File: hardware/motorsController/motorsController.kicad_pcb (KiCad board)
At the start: 2 copper layers, 181 x 55.5 mm, 80 parts, among them J1 batery_connector, J10 batery_connector, J11 Conn_01x04, J2 Screw_Terminal_01x01, J3 Screw_Terminal_01x01, J4 Screw_Terminal_01x01, J5 Screw_Terminal_01x01, J6 Screw_Terminal_01x01, J7 Screw_Terminal_01x01, J8 Screw_Terminal_01x01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

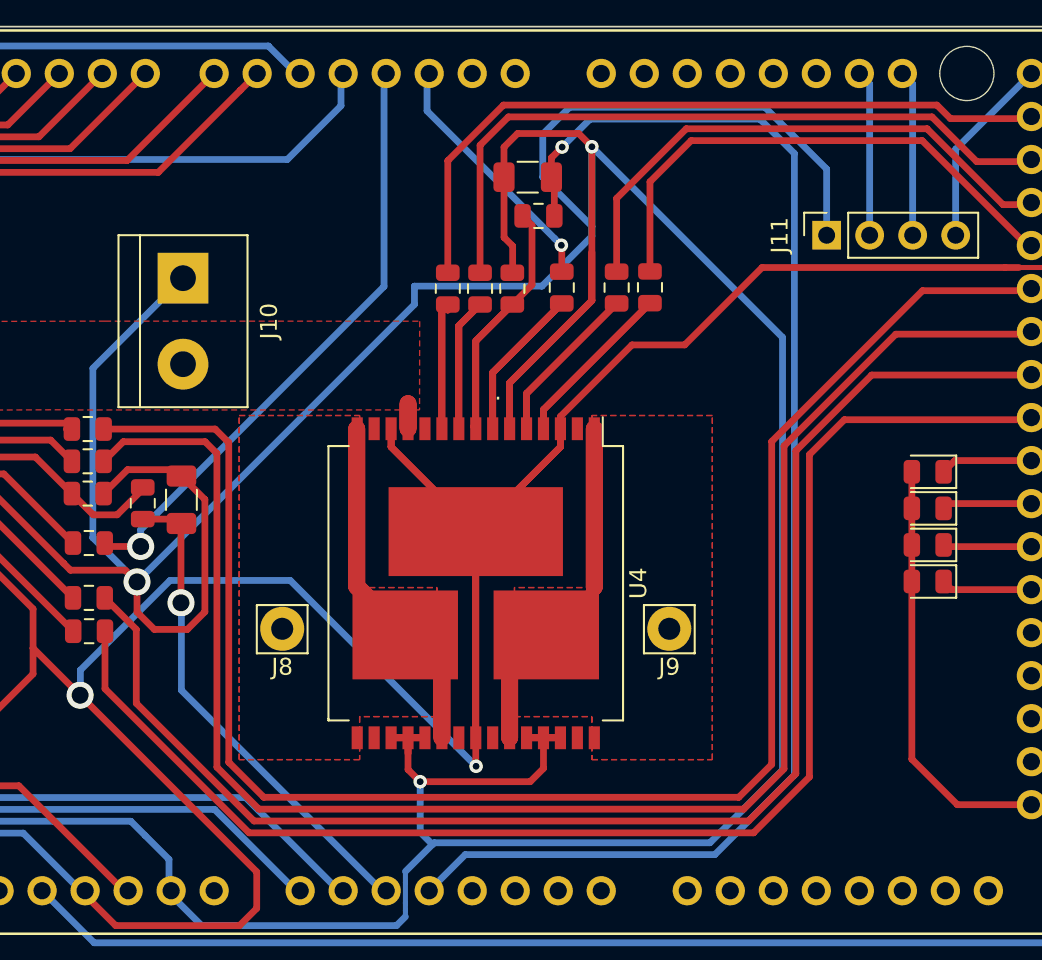
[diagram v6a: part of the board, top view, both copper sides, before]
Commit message: increase vias' dieamter for rear-left driver
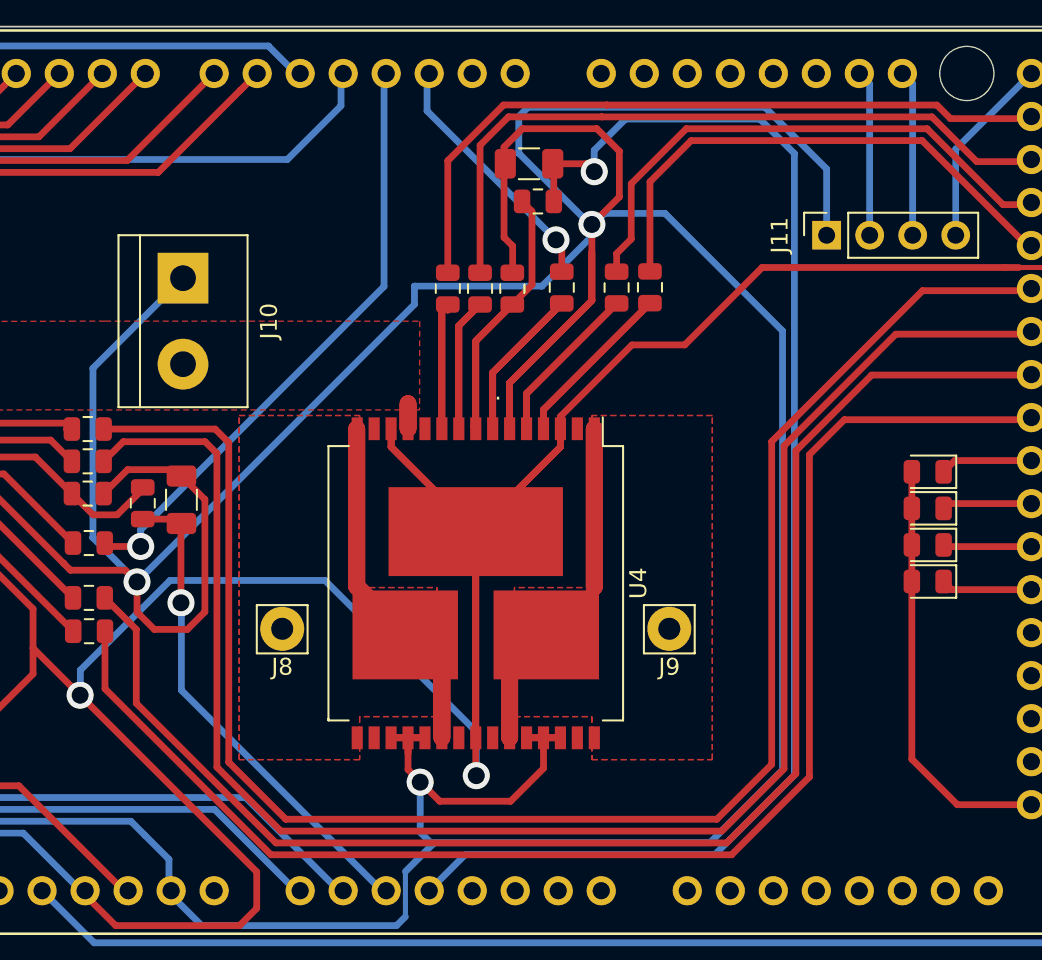
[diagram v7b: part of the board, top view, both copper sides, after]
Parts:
- moved R22 0.86 mm to (162.1, 34.5)
- moved C4 0.80 mm to (161.6, 32.2)
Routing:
- net +5V: track 422.7 -> 425.0 mm
- net /motor_right_rear_diag_b: track 97.8 -> 98.8 mm
- net /motor_right_rear_fwd: track 82.8 -> 83.8 mm
- net /motor_right_rear_diag_a: track 84.7 -> 85.8 mm
- net /motor_right_rear_back: track 98.3 -> 99.4 mm
- net Net-(R22-Pad1): track 22.8 -> 23.6 mm
- net /motor_left_rear_pwm: track 14.9 -> 15.5 mm

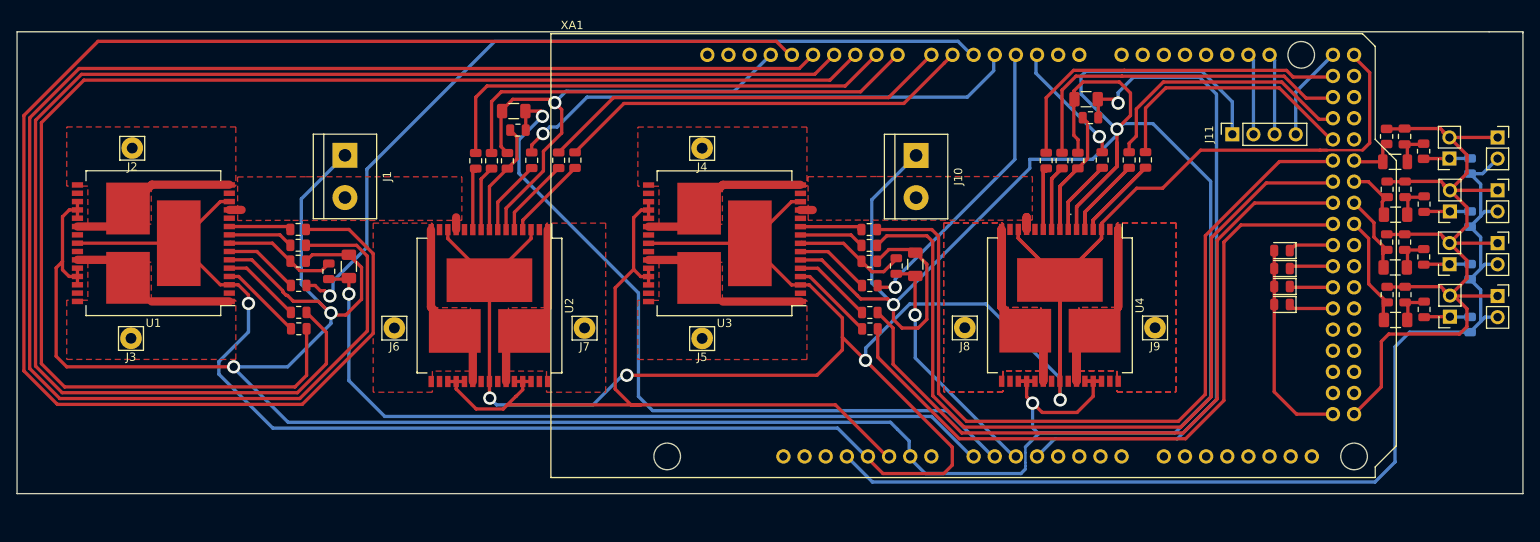
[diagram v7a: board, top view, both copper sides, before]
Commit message: layout a pcb for testing a motor driver
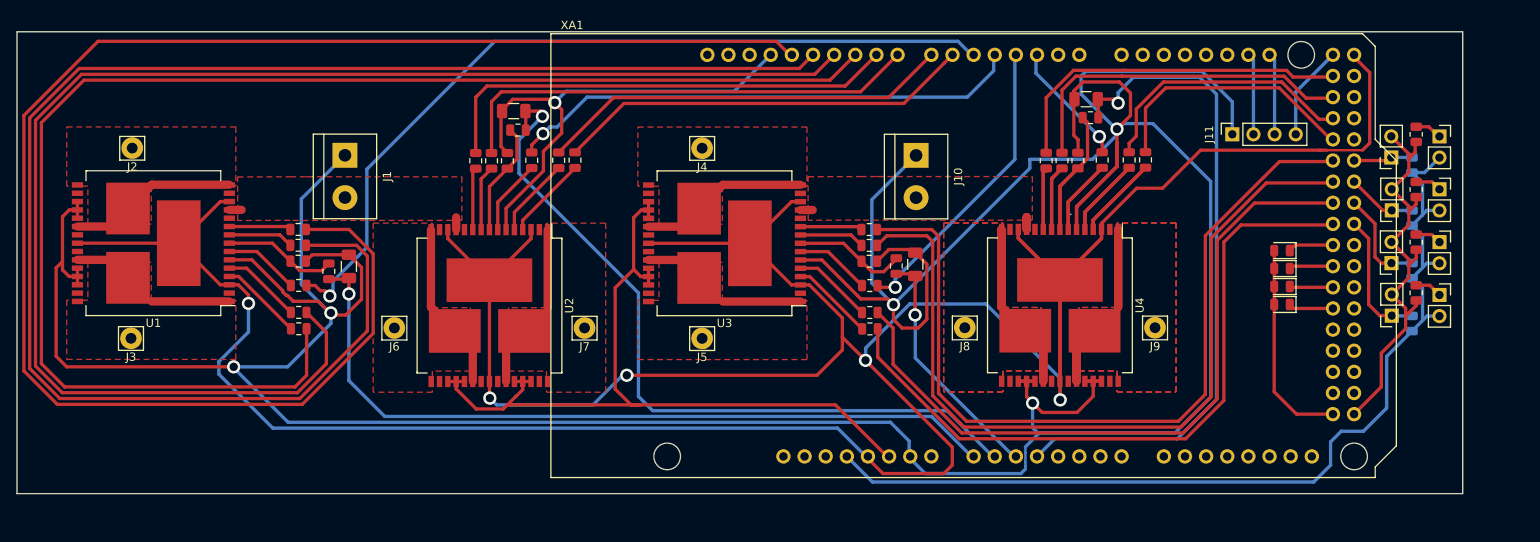
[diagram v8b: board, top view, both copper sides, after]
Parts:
- removed C10, C12, C6, C8: 82nF, Capacitor_SMD:C_1206_3216Metric
- removed C11, C5, C7, C9: 300pF, Capacitor_SMD:C_0805_2012Metric
- removed R33, R34, R35, R36: 2M, Resistor_SMD:R_0805_2012Metric
- R29, R30, R31, R32: value 2M -> 50
- moved R31 10.7 mm to (201.3, 55.5)
- moved R30 7.30 mm to (201.3, 43.1), turned to 270 degrees
- moved R32 7.24 mm to (201.3, 49.4), turned to 270 degrees
- moved D1 6.99 mm to (204.1, 36.7)
- moved D2 6.99 mm to (204.1, 43.1)
- moved D3 6.99 mm to (204.1, 55.8)
- moved D4 6.99 mm to (204.1, 49.4)
- moved Q1 6.99 mm to (198.3, 39.2)
- moved Q2 6.99 mm to (198.4, 45.6)
- moved Q3 6.99 mm to (198.3, 51.9)
- moved Q4 6.99 mm to (198.4, 58.2)
- moved R37 6.99 mm to (200.8, 40.1)
- moved R38 6.99 mm to (200.8, 46.5)
- moved R39 6.99 mm to (200.8, 52.8)
- moved R40 6.99 mm to (200.8, 59.2)
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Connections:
- D1 pad 1: GND -> Net-(D1-Pad1)
- D2 pad 1: GND -> Net-(D2-Pad1)
- D3 pad 1: GND -> Net-(D3-Pad1)
- D4 pad 1: GND -> Net-(D4-Pad1)
- Q1 pad 1: Net-(Q1-Pad1) -> /front_right_encoder
- Q2 pad 1: Net-(Q2-Pad1) -> /front_left_encoder
- Q3 pad 1: Net-(Q3-Pad1) -> /rear_right_encoder
- Q4 pad 1: Net-(Q4-Pad1) -> /rear_left_encoder
- R29 pad 1: Net-(C5-Pad1) -> Net-(D1-Pad1)
- R29 pad 2: Net-(Q1-Pad1) -> GND
- R30 pad 1: /front_right_encoder -> Net-(D2-Pad1)
- R31 pad 1: Net-(C7-Pad1) -> Net-(D3-Pad1)
- R31 pad 2: Net-(Q2-Pad1) -> GND
- R32 pad 1: /front_left_encoder -> Net-(D4-Pad1)
- R37 pad 2: Net-(Q1-Pad1) -> /front_right_encoder
- R38 pad 2: Net-(Q2-Pad1) -> /front_left_encoder
- R39 pad 2: Net-(Q3-Pad1) -> /rear_right_encoder
- R40 pad 2: Net-(Q4-Pad1) -> /rear_left_encoder
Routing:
- net GND: track 775.9 -> 718.0 mm
- net +3V3: track 125.3 -> 115.6 mm
- net Net-(Q1-Pad1): track 5.62 -> 0.00 mm
- net Net-(Q3-Pad1): track 5.60 -> 0.00 mm
- net Net-(Q4-Pad1): track 5.57 -> 0.00 mm
- net Net-(Q2-Pad1): track 5.56 -> 0.00 mm
- net Net-(C11-Pad1): track 4.56 -> 0.00 mm
- net Net-(C7-Pad1): track 4.56 -> 0.00 mm
- net Net-(C5-Pad1): track 4.56 -> 0.00 mm
- net Net-(C10-Pad2): track 4.56 -> 0.00 mm
- net Net-(D2-Pad1): track 0.00 -> 3.35 mm
- net Net-(D1-Pad1): track 0.00 -> 3.29 mm
- net Net-(D3-Pad1): track 0.00 -> 3.28 mm
- net Net-(D4-Pad1): track 0.00 -> 3.17 mm
- net /rear_left_encoder: track 13.4 -> 16.2 mm
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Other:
- board size 181 x 55.5 mm -> 173.7 x 55.5 mm
